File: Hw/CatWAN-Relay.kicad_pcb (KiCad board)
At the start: 2 copper layers, 224.8 x 100 mm, 61 parts, among them J1 24v, J10 USB_B, J2 Output 3, J3 Input 1, J4 SWD, J5 Serial, J6 Output 2, J7 Output 1, J8 Input 2, J9 Input 3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

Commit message: First route
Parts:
- removed G***: LOGO, agroin:electronic_cats_logo_8x6
- removed J1: 24v, agroin:691313710002
- removed J6: Output 2, agroin:691313710003
- removed J7: Output 1, agroin:691313710003
- removed J8: Input 2, agroin:691313710002
- removed J9: Input 3, agroin:691313710002
- removed MK1, MK2, MK3, MK4: Mounting_Hole, Mounting_Holes:MountingHole_3.5mm_Pad_Via
- removed REF** (x2): TerminalBlock_Phoenix_MKDS-1,5-9-5.08_1x09_P5.08mm_Horizont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, TerminalBlock_Phoenix:TerminalBlock_Phoenix_MKDS-1,5-9-5.08_1x09_P5.08mm_Horizontal
- removed REF** (x2): TerminalBlock_Phoenix_MKDS-1,5-6-5.08_1x06_P5.08mm_Horizont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, TerminalBlock_Phoenix:TerminalBlock_Phoenix_MKDS-1,5-6-5.08_1x06_P5.08mm_Horizontal
- removed REF***: WEEE-Logo_4.2x6mm_SilkScreen, Symbols:WEEE-Logo_4.2x6mm_SilkScreen
- AE1: footprint SMA_EDGE -> Connectors:MOLEX_1661
- C1, C3, C4, C5, C6, C7: footprint Capacitors_SMD:C_0805_HandSoldering -> Capacitor_SMD:C_0805_2012Metric_Pad1.15x1.40mm_HandSolder
- C2: footprint Capacitors_SMD:c_elec_6.3x7.7 -> Capacitor_SMD:C_Elec_6.3x7.7
- D4: footprint Diodes_SMD:D_SOD-123 -> Diode_SMD:D_SOD-123
- D5: footprint Diodes_SMD:SOD-123 -> Diode_SMD:D_SOD-123
- D6, D7: footprint LEDs:LED_0805_HandSoldering -> LED_SMD:LED_0805_2012Metric_Pad1.15x1.40mm_HandSolder
- J2: value Output 3 -> INPUTS; footprint agroin:691313710003 -> TerminalBlock_Phoenix:TerminalBlock_Phoenix_MKDS-1,5-9-5.08_1x09_P5.08mm_Horizontal
- J3: value Input 1 -> OUTPUTS; footprint agroin:691313710002 -> TerminalBlock_Phoenix:TerminalBlock_Phoenix_MKDS-1,5-9-5.08_1x09_P5.08mm_Horizontal
- J4: footprint Pin_Headers:Pin_Header_Straight_1x04_Pitch2.54mm -> Connector_PinHeader_2.54mm:PinHeader_1x04_P2.54mm_Vertical
- J5: footprint Pin_Headers:Pin_Header_Straight_1x03_Pitch2.54mm -> Connector_PinHeader_2.54mm:PinHeader_1x03_P2.54mm_Vertical
- JP1: footprint Pin_Headers:Pin_Header_Straight_1x02_Pitch2.54mm -> Connector_PinHeader_2.54mm:PinHeader_1x02_P2.54mm_Vertical
- Q1, Q2, Q3: footprint TO_SOT_Packages_SMD:SOT-23 -> Package_TO_SOT_SMD:SOT-23
- R1, R10, R11, R2, R3, R4, R5, R6, R7, R8, R9: footprint Resistors_SMD:R_0805_HandSoldering -> Resistor_SMD:R_0805_2012Metric_Pad1.15x1.40mm_HandSolder
- SW1: footprint Buttons_Switches_SMD:SW_SPST_B3U-1000P -> Button_Switch_SMD:SW_SPST_TL3342
- U1: footprint Housings_QFP:TQFP-32_7x7mm_Pitch0.8mm -> Package_QFP:TQFP-32_7x7mm_P0.8mm
- U3, U4, U5: footprint Housings_DIP:DIP-4_W7.62mm -> Package_DIP:DIP-4_W7.62mm_Socket
- U7: footprint TO_SOT_Packages_SMD:SOT-223-3Lead_TabPin2 -> Package_TO_SOT_SMD:SOT-223-3_TabPin2
- moved D6 92.3 mm to (134.3, 135.6), turned to 90 degrees
- moved J2 89.3 mm to (122.4, 70.4), turned to 0 degrees
- moved R9 83.9 mm to (134.3, 131.5), turned to 270 degrees
- moved D7 80.6 mm to (150.2, 136.2), turned to 90 degrees
- moved C4 79.0 mm to (129.3, 118.3), turned to 270 degrees
- moved J4 75.6 mm to (119.7, 120.3), turned to 0 degrees
- moved SW1 74.7 mm to (150.1, 125.2)
- moved J3 72.2 mm to (122.2, 146.0), turned to 0 degrees
- moved R11 70.5 mm to (150.1, 131.7), turned to 270 degrees
- moved C3 69.6 mm to (127.0, 118.3), turned to 270 degrees
- moved J10 61.9 mm to (122.7, 113.6), turned to 270 degrees
- moved AE1 56.5 mm to (165.5, 103.7)
- moved U1 52.5 mm to (136.5, 114.8), turned to 90 degrees
- moved Y1 51.7 mm to (123.0, 129.0), turned to 0 degrees
- moved C6 51.1 mm to (127.5, 110.0), turned to 180 degrees
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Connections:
- J2 pad 1: /NO1 -> GND
- J2 pad 2: /COM1 -> GND
- J2 pad 3: /NC1 -> /IC2
- J3 pad 1: GND -> /NO1
- J3 pad 2: /IA2 -> /COM1
- R4 pad 2: /DI1 -> /DI3
- R7 pad 2: /DI3 -> /DI1
- U3 pad 4: /DI1 -> /DI3
- U5 pad 4: /DI3 -> /DI1
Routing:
- net +3V3: track 327.2 -> 222.5 mm, vias 4 -> 7
- net /DI1: track 32.5 -> 96.8 mm, vias 0 -> 1
- net /DO3: track 75.6 -> 23.9 mm
- net /DI2: track 41.5 -> 90.8 mm, vias 0 -> 1
- net GND: track 99.7 -> 50.4 mm, vias 37 -> 7
- net /DO2: track 54.5 -> 6.65 mm
- net +24V: track 75.4 -> 37.5 mm
- net /COM3: track 0.00 -> 35.3 mm
- net /DI3: track 53.4 -> 84.4 mm, vias 0 -> 1
- net /COM2: track 0.00 -> 30.1 mm
- net /RST: track 14.0 -> 42.2 mm, vias 0 -> 2
- net /D-: track 40.3 -> 14.2 mm, vias 4 -> 2
- net /COM1: track 0.00 -> 22.7 mm
- net /D+: track 37.4 -> 14.9 mm, vias 4 -> 2
- net VBUS: track 26.4 -> 10.1 mm
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- removed copper zone on F.Cu, net /COM1
- removed copper zone on F.Cu, net /COM2
- removed copper zone on F.Cu, net /COM3
- removed copper zone on F.Cu, net /NC1
- removed copper zone on F.Cu, net /NC2
- removed copper zone on F.Cu, net /NC3
- removed copper zone on F.Cu, net /NO1
- removed copper zone on F.Cu, net /NO2
- removed copper zone on F.Cu, net /NO3
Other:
- board size 224.8 x 100 mm -> 50 x 86.9 mm
- net class Default: clearance 0.2 -> 0.3; trace_width 0.35 -> 0.3
- net class Vcc+: clearance 0.5 -> 0.2; trace_width 0.75 -> 1.2
- net class usb added: clearance 0.2, trace_width 0.3, via_dia 0.8, via_drill 0.4
- net class vcc: clearance 0.35 -> 0.5; via_dia 0.9 -> 1; via_drill 0.45 -> 0.6
- rule trace_clearance: 0.2 -> 0.3
- board text removed: "+"
- board text removed: "-"
- board text removed: "3V3"
- board text removed: "C"
- board text removed: "CLK"
- board text removed: "Cat-Relay"
- board text removed: "DIO"
- board text removed: "GND"
- board text removed: "NC"
- board text removed: "NO"
- board text removed: "Rx"
- board text removed: "Tx"
- board text removed: "V0.8"

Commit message: Add_Diode
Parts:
- added D8: MBR120, Diode_SMD:D_SOD-123, F.Cu at (129.0, 94.0)
- R3, R6, R8: value 2.2k -> 330R
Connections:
- JP1 pad 1: Net-(JP1-Pad1) -> Net-(D8-Pad1)
- R3 pad 2: +24V -> +3V3
- R6 pad 2: +24V -> +3V3
- R8 pad 2: +24V -> +3V3
- U6 pad 3: Net-(JP1-Pad1) -> Net-(D8-Pad2)
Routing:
- net +24V: track 37.5 -> 4.14 mm
- net +3V3: track 222.5 -> 251.1 mm
- net Net-(D8-Pad1): track 0.00 -> 11.9 mm
- net Net-(D8-Pad2): track 0.00 -> 7.17 mm

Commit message: update labels and logos
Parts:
- added G***: LOGO, Aesthetics:electronic_cats_logo_4x3, F.Cu at (134.3, 124.8)
- added svg2mod: electronic, Aesthetics:titule_electronic_med, B.Cu at (138.3, 121.8)
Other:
- board text added: "CatWAN Relay v1.0"

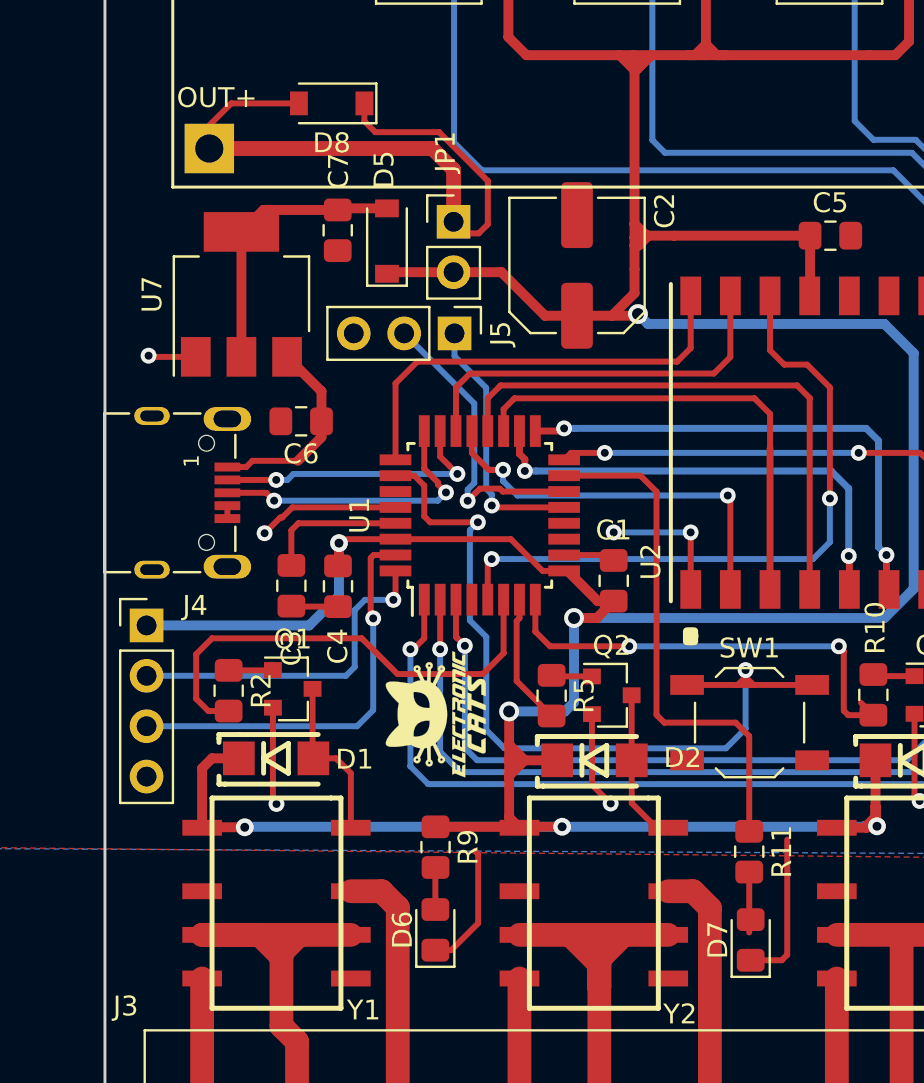
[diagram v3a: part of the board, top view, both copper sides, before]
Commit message: SWD SMD and fix labels
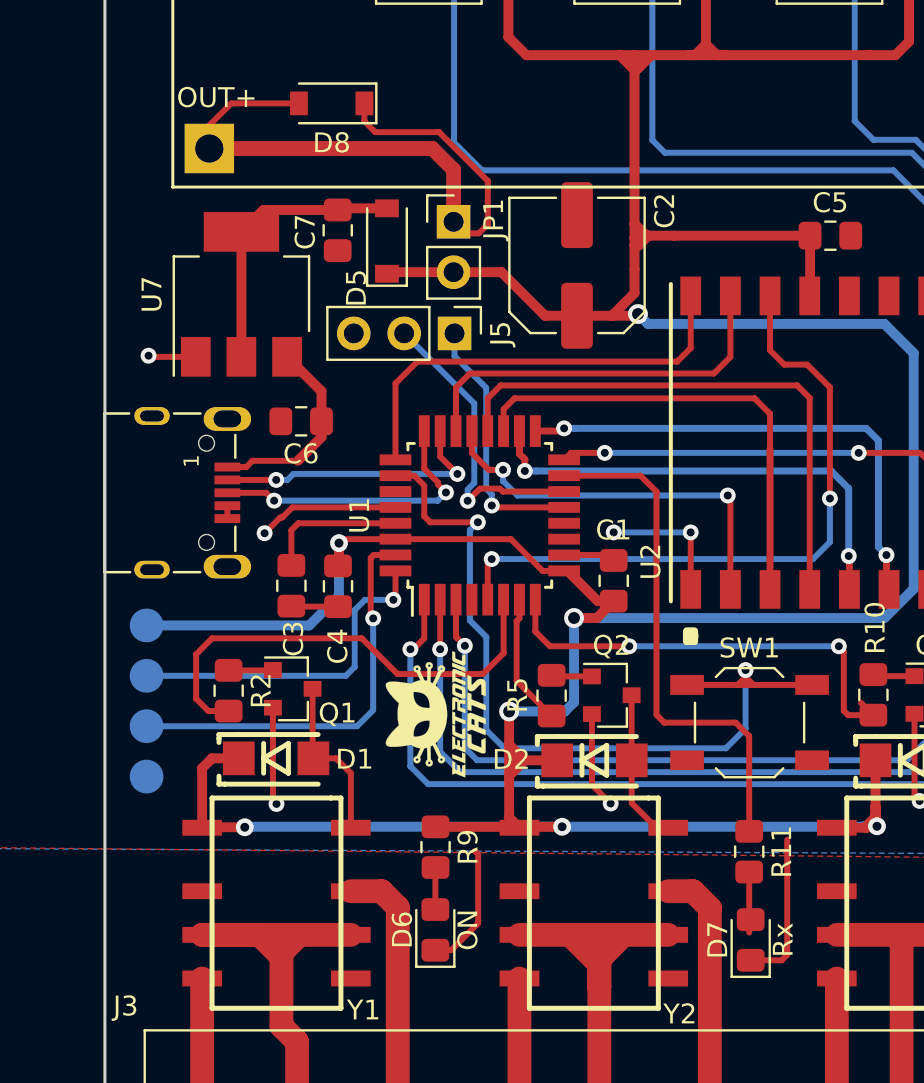
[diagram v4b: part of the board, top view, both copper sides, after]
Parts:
- J4: moved to B.Cu
- turned J4 to 180 degrees

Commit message: remove squematic oldversion
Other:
- net class Default removed
- net class Vcc+ removed
- net class usb removed
- net class vcc removed

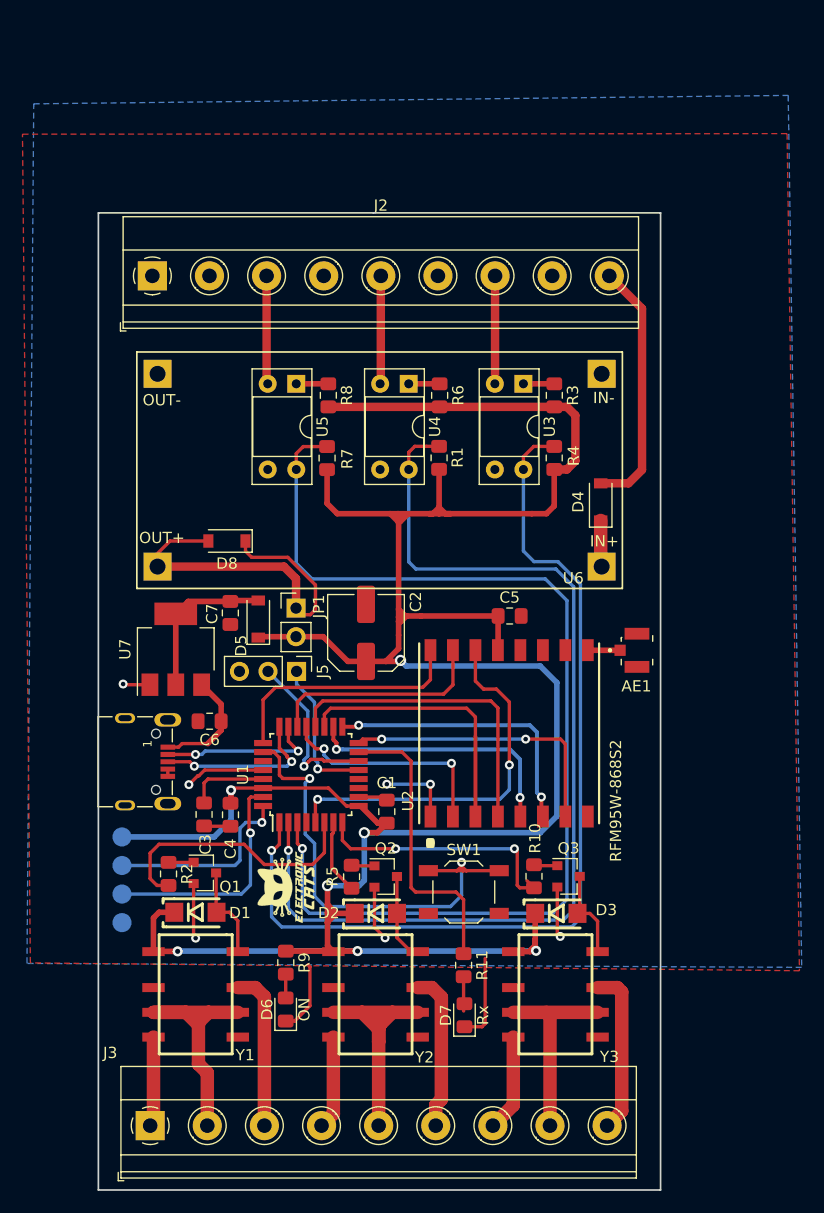
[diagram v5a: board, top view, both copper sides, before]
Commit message: feat(Hw):Update_sch_aadded_footprints_symbols
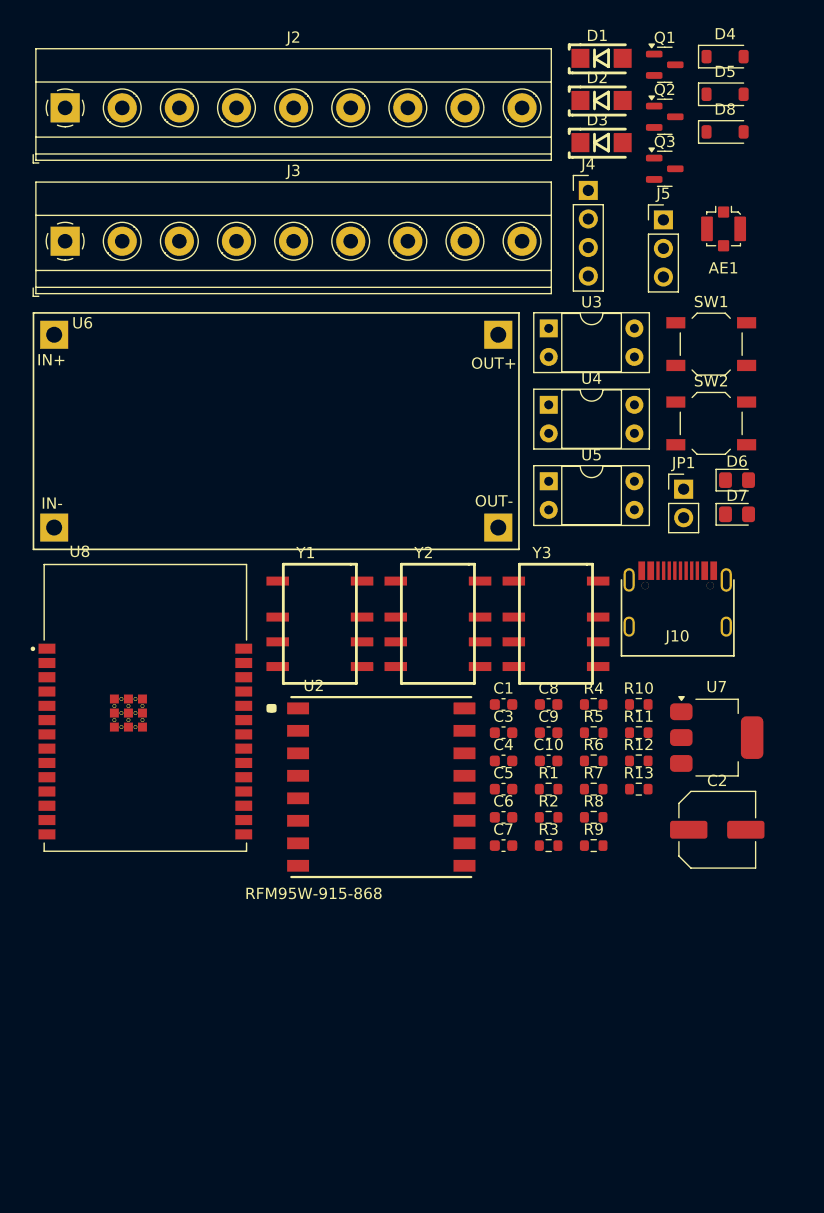
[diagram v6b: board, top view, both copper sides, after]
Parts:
- removed G***: LOGO, Aesthetics:electronic_cats_logo_4x3
- removed U1: ATSAMD21E, Package_QFP:TQFP-32_7x7mm_P0.8mm
- removed svg2mod: electronic, Aesthetics:titule_electronic_med
- added C10: 10uF, Capacitor_SMD:C_0603_1608Metric, F.Cu at (157.6, 113.5)
- added C8: 1uF, Capacitor_SMD:C_0603_1608Metric, F.Cu at (157.6, 108.5)
- added C9: 10uF, Capacitor_SMD:C_0603_1608Metric, F.Cu at (157.6, 111.0)
- added R12: 3.3K, Resistor_SMD:R_0603_1608Metric, F.Cu at (165.7, 113.5)
- added R13: 10K, Resistor_SMD:R_0603_1608Metric, F.Cu at (165.7, 116.0)
- added SW2: ~, Button_Switch_SMD:SW_SPST_TL3342, F.Cu at (172.1, 83.5)
- added U8: ESP32-C6-WROOM-1U-N4, agroin:XCVR_ESP32-C6-WROOM-1-N8, F.Cu at (121.8, 108.8)
- AE1: footprint Connectors:MOLEX_1661 -> Connector_Coaxial:U.FL_Molex_MCRF_73412-0110_Vertical
- C1, C4, C5, C6, C7: footprint Capacitor_SMD:C_0805_2012Metric_Pad1.15x1.40mm_HandSolder -> Capacitor_SMD:C_0603_1608Metric
- C3: value 1uF -> 0.1uF; footprint Capacitor_SMD:C_0805_2012Metric_Pad1.15x1.40mm_HandSolder -> Capacitor_SMD:C_0603_1608Metric
- J10: footprint USB:629105150521 -> agroin:C393939
- J4: moved to F.Cu
- R1, R10, R11, R2, R3, R4, R5, R6, R7, R8, R9: footprint Resistor_SMD:R_0805_2012Metric_Pad1.15x1.40mm_HandSolder -> Resistor_SMD:R_0603_1608Metric
- SW1: value RST -> ~
- U2: value RFM95W-868S2 -> RFM95W-915-868
- moved D1 84.1 mm to (160.5, 51.0)
- moved Q1 82.7 mm to (168.0, 51.6)
- moved J3 79.0 mm to (114.6, 67.3)
- moved D2 75.0 mm to (160.5, 54.8)
- moved Q2 72.0 mm to (168.0, 56.2)
- moved J4 70.9 mm to (161.2, 62.8), turned to 0 degrees
- moved D3 68.7 mm to (160.5, 58.5)
- moved Q3 63.5 mm to (168.0, 60.9)
- moved D5 62.5 mm to (173.3, 54.2), turned to 0 degrees
- moved D6 61.9 mm to (174.4, 88.6), turned to 0 degrees
- moved U6 57.8 mm to (111.8, 73.7), turned to 0 degrees
- moved D8 57.3 mm to (173.3, 57.6), turned to 0 degrees
- moved SW1 53.5 mm to (172.1, 76.5)
- moved J5 51.7 mm to (167.9, 65.4), turned to 0 degrees
- moved D7 50.7 mm to (174.4, 91.6), turned to 0 degrees
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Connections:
- C3 pad 1: Net-(C3-Pad1) -> GND
- C3 pad 2: GND -> /BOOT
- C4 pad 1: +3V3 -> GND
- C4 pad 2: GND -> /EN
- J4 pad 2: /SWDIO -> /SDA
- J4 pad 3: /SWCLK -> /SCL
- SW1 pad 1: /RST -> GND
- SW1 pad 2: GND -> /BOOT
- U2 pad 11: Net-(U2-Pad11) -> unconnected-(U2-DIO3-Pad11)
- U2 pad 12: Net-(U2-Pad12) -> unconnected-(U2-DIO4-Pad12)
- Y1 pad 4: Net-(Y1-Pad4) -> unconnected-(Y1-NA-Pad4)
- Y1 pad 7: Net-(Y1-Pad7) -> unconnected-(Y1-NC1-Pad7)
- Y2 pad 4: Net-(Y2-Pad4) -> unconnected-(Y2-NA-Pad4)
- Y2 pad 7: Net-(Y2-Pad7) -> unconnected-(Y2-NC1-Pad7)
- Y3 pad 4: Net-(Y3-Pad4) -> unconnected-(Y3-NA-Pad4)
- Y3 pad 7: Net-(Y3-Pad7) -> unconnected-(Y3-NC1-Pad7)
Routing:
- net +3V3: track 251.1 -> 0.00 mm, vias 7 -> 0
- net /DI1: track 96.8 -> 0.00 mm, vias 1 -> 0
- net /DI2: track 90.8 -> 0.00 mm, vias 1 -> 0
- net /DI3: track 84.4 -> 0.00 mm, vias 1 -> 0
- net GND: track 50.4 -> 0.00 mm, vias 7 -> 0
- net /RST: track 42.2 -> 0.00 mm, vias 2 -> 0
- net /COM3: track 35.3 -> 0.00 mm
- net /DIO0: track 33.9 -> 0.00 mm, vias 2 -> 0
- net /COM2: track 30.1 -> 0.00 mm
- net /SCK: track 28.1 -> 0.00 mm
- net /Rx_LED: track 26.2 -> 0.00 mm
- net /RFM_RST: track 25.3 -> 0.00 mm, vias 2 -> 0
- net /DIO5: track 25.2 -> 0.00 mm, vias 2 -> 0
- net /MOSI: track 23.9 -> 0.00 mm
- net /SS: track 23.9 -> 0.00 mm, vias 2 -> 0
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- removed copper zone on B.Cu, net GND
- removed copper zone on F.Cu, net GND
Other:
- board outline removed
- board text removed: "CatWAN Relay v1.0"
